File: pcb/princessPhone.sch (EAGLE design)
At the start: 75 parts, among them IC1 OPA2134UA, P2 TC2030-MCP-NL, Q1 2N7002K, SW3 LL1105BF250Q, SW4 LL1105BF250Q, SW5 LL1105BF250Q, SW6 LL1105BF250Q, U1 AG1170-S3-VERTICAL, U2 PI32MX170D-PT, U3 BLUETOOTH-RN-52, U4 V_REG_LD1085D2, X1 22-23-2041, X2 XRJK-S-01-6-4-0-9M2, X3 USB_MICRO_B

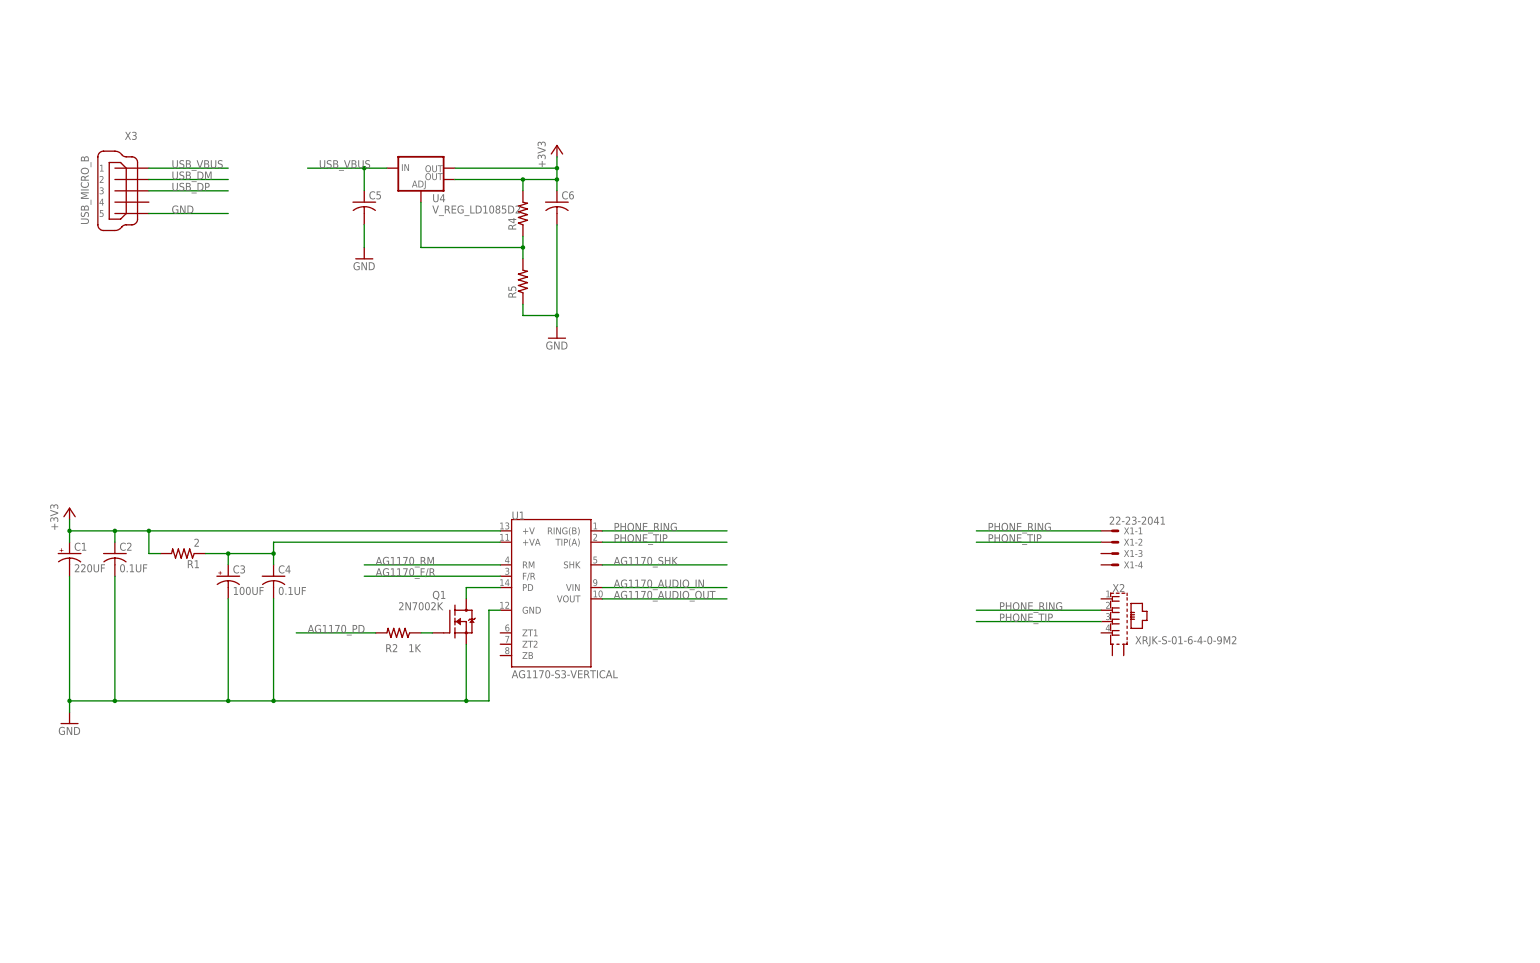
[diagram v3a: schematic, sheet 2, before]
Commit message: Replaced leo with switcher, finished first-pass layout, added LEDs.
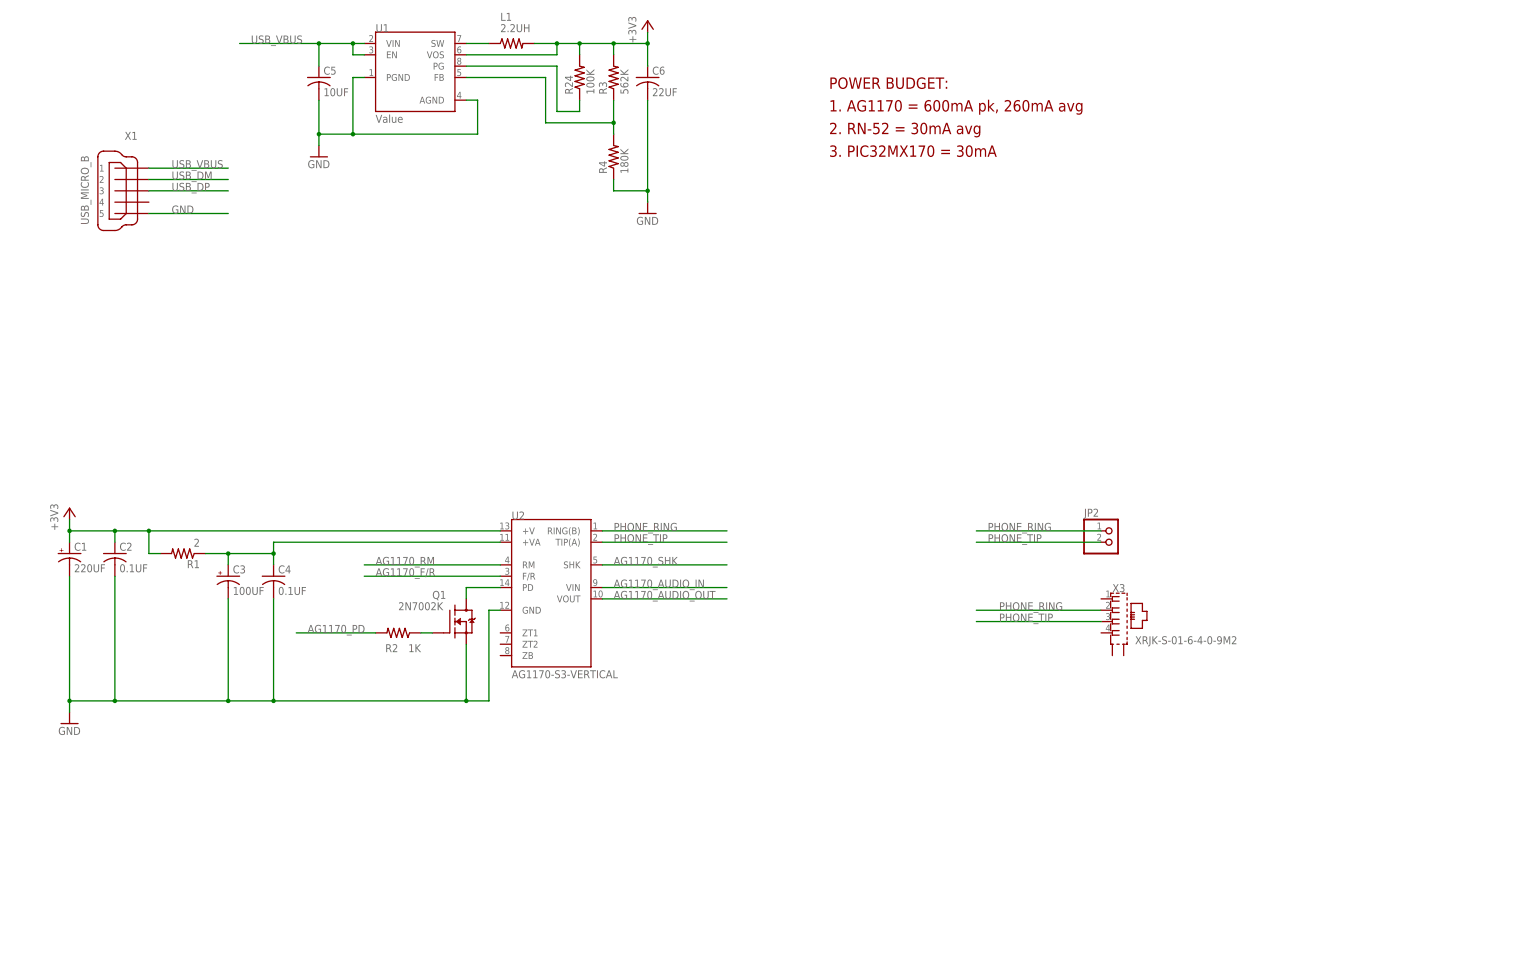
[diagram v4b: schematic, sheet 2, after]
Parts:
- removed C28: 0.1UF, rcl:C-USC0402
- removed IC1: OPA2134UA, linear:OPA2134UA
- removed R27, R28, R29: 10K, rcl:R-US_R0603
- removed SW5, SW6: LL1105BF250Q, raveGearControl:LL1105BF250Q
- removed TP3: PTR1B1,27, testpad:PTR1B1,27
- removed X2: XRJK-S-01-6-4-0-9M2, con-xmultiple:XRJK-S-01-6-4-0-9M2
- added C8: 0.1UF, rcl:C-USC0402
- added JP2: (no value), pinhead:PINHD-1X2
- added L1: 2.2UH, rcl:R-US_R0805
- added LED3: BLUE, led:LEDCHIPLED_0603
- added LED4: RED, led:LEDCHIPLED_0603
- added SW1, SW2: LL1105BF250Q, raveGearControl:LL1105BF250Q
- C2, C4: device rcl:C-USC0805 -> rcl:C-USC0603
- C5: value (none) -> 10UF; device rcl:C-USC0603 -> rcl:C-USC0805
- C6: value (none) -> 22UF; device rcl:C-USC0603 -> rcl:C-USC1206
- R10: value NP -> 10K
- R11: value 47K -> 10K
- R13: value NP -> 47K
- R14, R20, R21: value NP -> 0
- R15, R16, R17: value 47 -> 0
- R19: value NP -> 470
- R24: value 0 -> 100K
- R25: value 0 -> 47
- R26: value 10K -> 470
- R3: value 10K -> 562K; device rcl:R-US_R0402 -> rcl:R-US_R0603
- R4: value (none) -> 180K
- R5: value (none) -> 10K; device rcl:R-US_R0603 -> rcl:R-US_R0402
- R7: value 47 -> 10K; device rcl:R-US_R0603 -> rcl:R-US_R0402
- R8: device rcl:R-US_R0402 -> rcl:R-US_R0603
- R9: value 470 -> 10K
- U1: value AG1170-S3-VERTICAL -> Value; device princessPhone:AG1170-S3-VERTICAL -> princessPhone:TPS62160DGKR
- U2: value PI32MX170D-PT -> AG1170-S3-VERTICAL; device raveGear5:PI32MX170D-PT -> princessPhone:AG1170-S3-VERTICAL
- U3: value BLUETOOTH-RN-52 -> PI32MX170D-PT; device SparkFun-RF:BLUETOOTH-RN-52 -> raveGear5:PI32MX170D-PT
- U4: value V_REG_LD1085D2 -> BLUETOOTH-RN-52; device SparkFun-PowerIC:V_REG_LD1085D2 -> SparkFun-RF:BLUETOOTH-RN-52
- X1: value 22-23-2041 -> USB_MICRO_B; device con-molex:22-23-2041 -> FosBattery1:USB_MICRO_B
- X3: value USB_MICRO_B -> XRJK-S-01-6-4-0-9M2; device FosBattery1:USB_MICRO_B -> con-xmultiple:XRJK-S-01-6-4-0-9M2
- renumbered C26 to C7, C27 to C9, P2 to P1
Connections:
- removed net PIC32_RSVD_10: TP3.TP, U2PORTB.RPB9/SDA1/CTED4/PMD3/RB9
- removed net RN52_SPKR_SUM: IC1A.+IN, R13.2, R14.2, R15.1
- new net N$5: L1.1, U1.SW
- new net N$6: R24.1, U1.PG
- new net N$7: LED3.C, R25.2
- net +3V3: now also C8.1, L1.2, LED3.A, LED4.A, R10.1, R11.1, R24.2, R5.2, R7.2, R8.1, R9.1, U1.VOS, U2.+V, U3PWR.AVDD, U3PWR.VDD@1, U3PWR.VDD@2, U4.VDD; no longer C28.1, IC1A.V+, R26.1, R27.1, R28.1, R29.1, R4.2, R8.2, U1.+V, U2PWR.AVDD, U2PWR.VDD@1, U2PWR.VDD@2, U3.VDD, U4.OUT, U4.OUT@1
- net AG1170_AUDIO_IN: now also U2.VIN; no longer IC1A.OUT, R15.2, U1.VIN
- net AG1170_AUDIO_OUT: now also R20.2, R21.2, U2.VOUT; no longer IC1B.+IN, R18.2, R24.2, R25.2, U1.VOUT
- net AG1170_F/R: now also U2.F/R, U3PORTC.RPC4/PMA4/RC4; no longer U1.F/R, U2PORTC.RPC4/PMA4/RC4
- net AG1170_PD: now also U3PORTC.RPC6/PMA1/RC6; no longer U2PORTC.RPC6/PMA1/RC6
- net AG1170_RM: now also U2.RM, U3PORTC.RPC3/RC3; no longer U1.RM, U2PORTC.RPC3/RC3
- net AG1170_SHK: now also U2.SHK, U3PORTC.RPC5/PMA3/RC5; no longer U1.SHK, U2PORTC.RPC5/PMA3/RC5
- net GND: now also C8.2, R13.1, R14.2, R15.2, R16.2, R17.2, R4.1, SW1.P, SW2.P, U1.AGND, U1.PGND, U2.GND, U3PWR.AVSS, U3PWR.VSS@1, U3PWR.VSS@2, U3PWR.VSS@3, U4.AGND, U4.GND, U4.GND1, U4.GND2, U4.GND3, U4.GND4, U4.GND5, U4.GND6, U4.GND7, U4.GND8, U4.GND9, X1.5; no longer C28.2, IC1A.-IN, IC1A.V-, IC1B.-IN, R10.2, R11.1, R19.2, R20.2, R21.2, R5.1, SW5.P, SW6.P, U1.GND, U2PWR.AVSS, U2PWR.VSS@1, U2PWR.VSS@2, U2PWR.VSS@3, U3.AGND, U3.GND, U3.GND1, U3.GND2, U3.GND3, U3.GND4, U3.GND5, U3.GND6, U3.GND7, U3.GND8, U3.GND9, X3.5
- net LED0: now also R18.1, U4.LED0; no longer R7.1, U3.LED0
- net LED1: now also R19.1, U4.LED1; no longer R9.1, U3.LED1
- net MCLR#: now also R5.1, U3PWR.#MCLR; no longer R3.1, U2PWR.#MCLR
- net N$1: now also U2.+VA; no longer U1.+VA
- net N$10: now also R19.2; no longer R9.2
- net N$11: now also U4.MIC_BIAS; no longer U3.MIC_BIAS
- net N$12: now also LED4.C, R26.2; no longer IC1B.OUT, R16.2, R17.2, R18.1
- net N$3: now also U2.PD; no longer U1.PD
- net N$4: now also U3PWR.VCAP; no longer U2PWR.VCAP
- net N$8: now also R3.1, R4.2, U1.FB; no longer R4.1, R5.2, U4.ADJ
- net N$9: now also R18.2; no longer R7.2
- net PHONE_RING: now also JP2.1, U2.RING(B), X3.2; no longer U1.RING(B), X1-1.S, X2.2
- net PHONE_TIP: now also JP2.2, U2.TIP(A), X3.3; no longer U1.TIP(A), X1-2.S, X2.3
- net PIC32_PGEC1: now also U3PORTB.PGEC1/AN3/C1INC/C2INA/RPB1/CTED12/RB1; no longer U2PORTB.PGEC1/AN3/C1INC/C2INA/RPB1/CTED12/RB1
- net PIC32_PGED1: now also U3PORTB.PGED1/AN2/C1IND/C2INB/C3IND/RPB0/RB0; no longer U2PORTB.PGED1/AN2/C1IND/C2INB/C3IND/RPB0/RB0
- net PIC32_RSVD_1: now also U3PORTA.VREF+/CVREF+/AN0/C3INC/RPA0/CTED1/RA0; no longer U2PORTA.VREF+/CVREF+/AN0/C3INC/RPA0/CTED1/RA0
- net PIC32_RSVD_11: now also U3PORTB.PGEC2/RPB11/PMD1/RB11; no longer U2PORTB.PGEC2/RPB11/PMD1/RB11
- net PIC32_RSVD_12: now also U3PORTB.CVREFOUT/AN10/C3INB/RPB14/SCK1/CTED5/PMWR/RB14; no longer U2PORTB.CVREFOUT/AN10/C3INB/RPB14/SCK1/CTED5/PMWR/RB14
- net PIC32_RSVD_2: now also U3PORTA.OSC1/CLKI/RPA2/RA2; no longer U2PORTA.OSC1/CLKI/RPA2/RA2
- net PIC32_RSVD_3: now also U3PORTA.OSC2/CLKO/RPA3/RA3; no longer U2PORTA.OSC2/CLKO/RPA3/RA3
- net PIC32_RSVD_4: now also U3PORTA.SOSCO/RPA4/T1CK/CTED9/RA4; no longer U2PORTA.SOSCO/RPA4/T1CK/CTED9/RA4
- net PIC32_RSVD_5: now also R26.1, U3PORTA.PGEC/TCK/CTED8/PMA7/RA7; no longer U2PORTA.PGEC/TCK/CTED8/PMA7/RA7
- net PIC32_RSVD_6: now also U3PORTA.TDO/RPA8/PMA8/RA8; no longer U2PORTA.TDO/RPA8/PMA8/RA8
- net PIC32_RSVD_7: now also U3PORTA.TDI/RPA9/PMA9/RA9; no longer U2PORTA.TDI/RPA9/PMA9/RA9
- net PIC32_RSVD_8: now also R25.1, U3PORTA.PGED/TMS/PMA10/RA10; no longer U2PORTA.PGED/TMS/PMA10/RA10
- net PIC32_RSVD_9: now also U3PORTB.SOSCI/RPB4/RB4; no longer U2PORTB.SOSCI/RPB4/RB4
- net PIC32_SCL2: now also R7.1, U3PORTB.AN5/C1INA/C2INC/RTCC/RPB3/SCL2/RB3; no longer R8.1, U2PORTB.AN5/C1INA/C2INC/RTCC/RPB3/SCL2/RB3
- net PIC32_SDA2: now also U3PORTB.AN4/C1INB/C2IND/RPB2/SDA2/CTED13/RB2; no longer U2PORTB.AN4/C1INB/C2IND/RPB2/SDA2/CTED13/RB2
- net PIC32_U1CTS#_3V3: now also U3PORTA.VREF-/CVREF-/AN1/RPA1/CTED2/RA1, U4.UART_RTS; no longer U2PORTA.VREF-/CVREF-/AN1/RPA1/CTED2/RA1, U3.UART_RTS
- net PIC32_U1RTS#_3V3: now also U3PORTB.PGED2/RPB10/CTED11/PMD2/RB10, U4.UART_CTS; no longer U2PORTB.PGED2/RPB10/CTED11/PMD2/RB10, U3.UART_CTS
- net PIC32_U1RX_3V3: now also U3PORTC.AN7/RPC1/RC1, U4.UART_TX; no longer U2PORTC.AN7/RPC1/RC1, U3.UART_TX
- net PIC32_U1TX_3V3: now also U3PORTC.AN6/RPC0/RC0, U4.UART_RX; no longer U2PORTC.AN6/RPC0/RC0, U3.UART_RX
- net RN52_CMD_MODE#: now also U3PORTC.RPC9/CTED7/PMA6/RC9, U4.GPIO9; no longer U2PORTC.RPC9/CTED7/PMA6/RC9, U3.GPIO9
- net RN52_DFU_MODE: now also R13.2, U3PORTB.RPB9/SDA1/CTED4/PMD3/RB9, U4.GPIO3; no longer R11.2, U3.GPIO3
- net RN52_EVENT#: now also U3PORTC.RPC8/PMA5/RC8, U4.GPIO2; no longer U2PORTC.RPC8/PMA5/RC8, U3.GPIO2
- net RN52_FACTORY_RST: now also U4.GPIO4; no longer U3.GPIO4
- net RN52_MIC_L+: now also R20.1, U4.MIC_L+; no longer R16.1, R24.1, R25.1, U3.MIC_L+
- net RN52_MIC_L-: now also R17.1, U4.MIC_L-; no longer R21.1, U3.MIC_L-
- net RN52_MIC_R+: now also R21.1, U4.MIC_R+; no longer R17.1, U3.MIC_R+
- net RN52_MIC_R-: now also R16.1, U4.MIC_R-; no longer R20.1, U3.MIC_R-
- net RN52_PWREN: now also U3PORTC.RPC7/PMA0/RC7, U4.PWREN; no longer U2PORTC.RPC7/PMA0/RC7, U3.PWREN
- net RN52_SPKR_L+: now also U4.SPKR_L+; no longer R13.1, U3.SPKR_L+
- net RN52_SPKR_L-: now also R14.1, U4.SPKR_L-; no longer R10.1, U3.SPKR_L-
- net RN52_SPKR_R+: now also U4.SPKR_R+; no longer R14.1, U3.SPKR_R+
- net RN52_SPKR_R-: now also R15.1, U4.SPKR_R-; no longer R19.1, U3.SPKR_R-
- net SST25_CE#: now also U3PORTB.AN12/PMD0/RB12; no longer U2PORTB.AN12/PMD0/RB12
- net SST25_MISO: now also U3PORTC.AN8/RPC2/PMA2/RC2; no longer U2PORTC.AN8/RPC2/PMA2/RC2
- net SST25_MOSI: now also U3PORTB.AN11/RPB13/CTPLS/PMRD/RB13; no longer U2PORTB.AN11/RPB13/CTPLS/PMRD/RB13
- net SST25_SCK: now also U3PORTB.AN9/C3INA/RPB15/SCK2/CTED6/PMCS1/RB15; no longer U2PORTB.AN9/C3INA/RPB15/SCK2/CTED6/PMCS1/RB15
- net SW0: now also R8.2, SW1.S, U3PORTB.PGED3/RPB5/PMD7/RB5; no longer R26.2, SW3.S, U2PORTB.PGED3/RPB5/PMD7/RB5
- net SW1: now also R9.2, SW2.S, U3PORTB.PGEC3/RPB6/PMD6/RB6; no longer R27.2, SW4.S, U2PORTB.PGEC3/RPB6/PMD6/RB6
- net SW2: now also R10.2, SW3.S, U3PORTB.RPB7/CTED3/PMD5/INT0/RB7; no longer R28.2, SW5.S, U2PORTB.RPB7/CTED3/PMD5/INT0/RB7
- net SW3: now also R11.2, SW4.S, U3PORTB.RPB8/SCL1/CTED10/PMD4/RB8; no longer R29.2, SW6.S, U2PORTB.RPB8/SCL1/CTED10/PMD4/RB8
- net USB_DM: now also U4.USBD-, X1.2; no longer U3.USBD-, X3.2
- net USB_DP: now also U4.USBD+, X1.3; no longer U3.USBD+, X3.3
- net USB_VBUS: now also U1.EN, X1.1; no longer U4.IN, X3.1
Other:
- note added: "1. AG1170 = 600mA pk, 260mA avg"
- note added: "2. RN-52 = 30mA avg"
- note added: "2015.08.06"
- note added: "3. PIC32MX170 = 30mA"
- note added: "FIRST-PASS AT LAYOUT, REMOVED "NP" COMPONENTS, REPLACED LDO WITH SWITCHER, ADDED LEDS"
- note added: "POWER BUDGET:"
- note removed: "STUFF OPTION 2"
- moved on the sheet: C10, C5, C6, R13, R14, R15, R16, R17, R18, R19, R20, R21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

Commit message: FIRST PASS AT LAYOUT
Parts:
- removed TP4: PTR1B1,27, testpad:PTR1B1,27
- added TP3: PTR1B1,27, testpad:PTR1B1,27
- JP1: device pinhead:PINHD-1X3 -> pinhead:PINHD-1X4
- LED3: value BLUE -> GREEN
- LED4: value RED -> YELLOW
- R25: value 47 -> 150
- R26: value 470 -> 150
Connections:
- removed net AG1170_AUDIO_IN_AGG: R22.1, R23.2
- removed net PIC32_RSVD_11: TP4.TP, U3PORTB.PGEC2/RPB11/PMD1/RB11
- net +3V3: now also JP1.1
- net AG1170_AUDIO_IN: now also R22.1, R23.2
- net GND: now also JP1.4; no longer JP1.1
- net PHONE_RING: now also X3.3; no longer X3.2
- net PHONE_TIP: now also X3.2; no longer X3.3
- net PIC32_U1RX_3V3: now also JP1.3; no longer JP1.2
- net PIC32_U1TX_3V3: now also JP1.2; no longer JP1.3
- net RN52_FACTORY_RST: now also U3PORTB.PGEC2/RPB11/PMD1/RB11
- net RN52_SPKR_R+: now also TP3.TP
- net USB_VBUS: now also U1.VIN
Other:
- note added: "4. LEDS = 10mA * 4 = 40mA"
- note added: "CONNECTED RN52 FACTORY RST LINE, CORRECTED RJ-11 PINOUT"
- note added: "FIRST-PASS AT LAYOUT"
- note added: "FIRST-PASS AT PLACEMENT, REMOVED "NP" COMPONENTS, REPLACED LDO WITH SWITCHER, ADDED LEDS"
- note removed: "FIRST-PASS AT LAYOUT, REMOVED "NP" COMPONENTS, REPLACED LDO WITH SWITCHER, ADDED LEDS"
- moved on the sheet: LED3, LED4, R25, R26

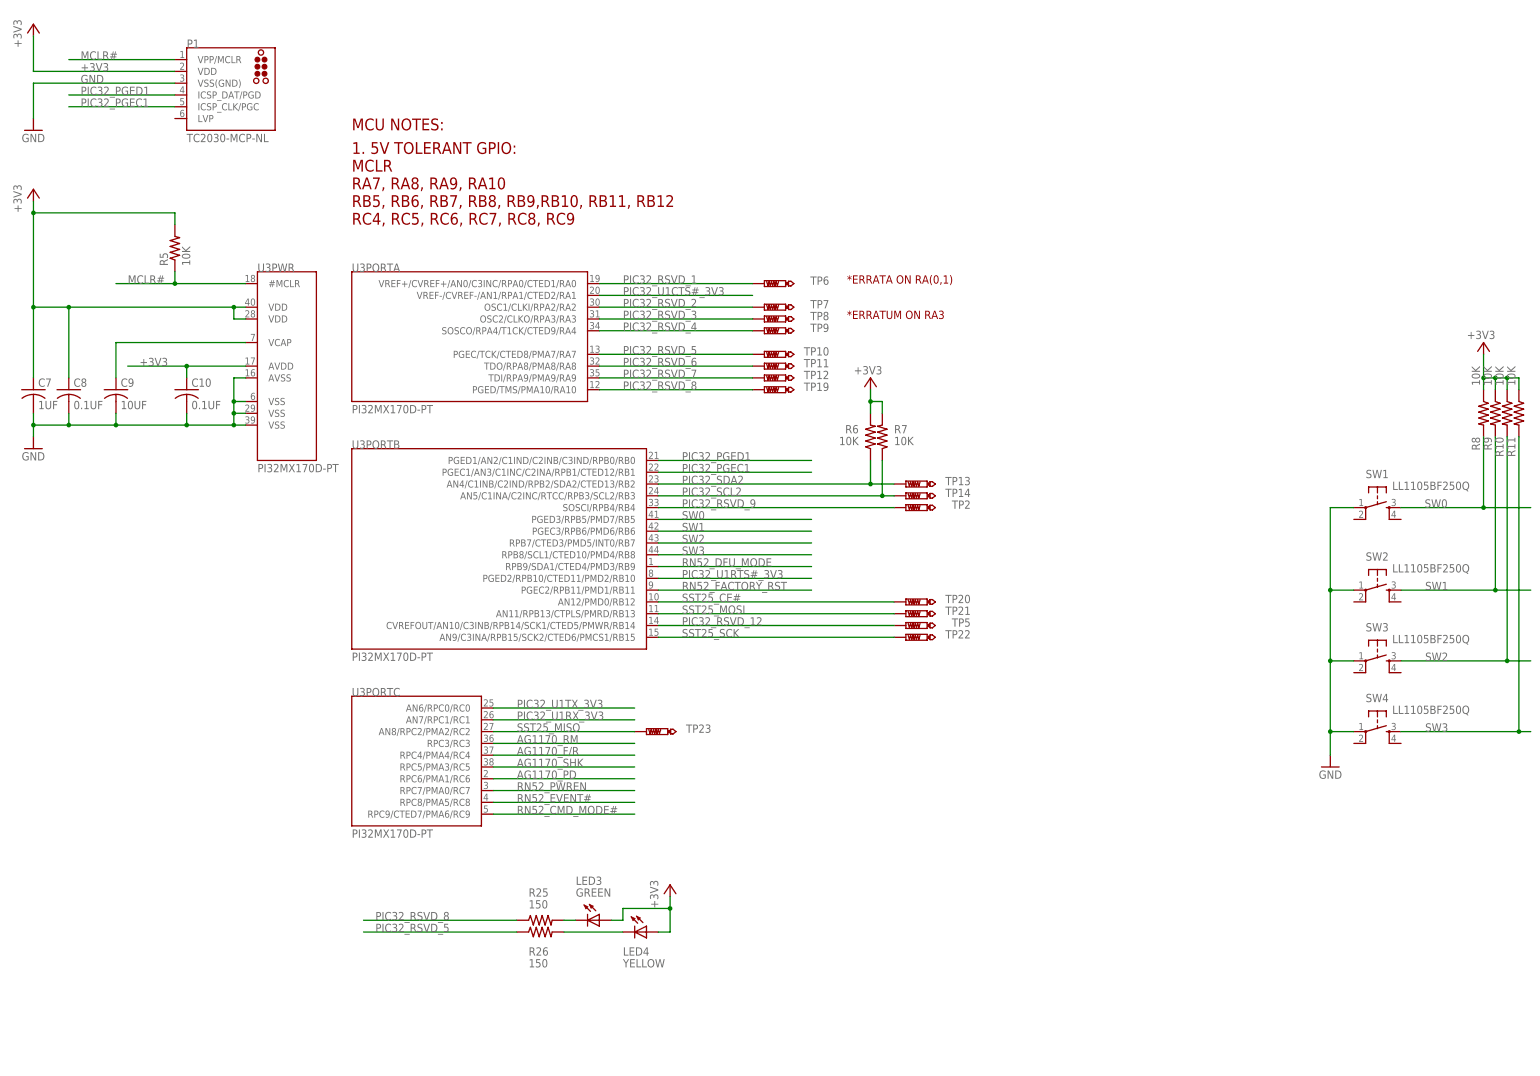
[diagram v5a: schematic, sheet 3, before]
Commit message: REMOVED BTN, ADDING LEDS, ADDED OUTLINE
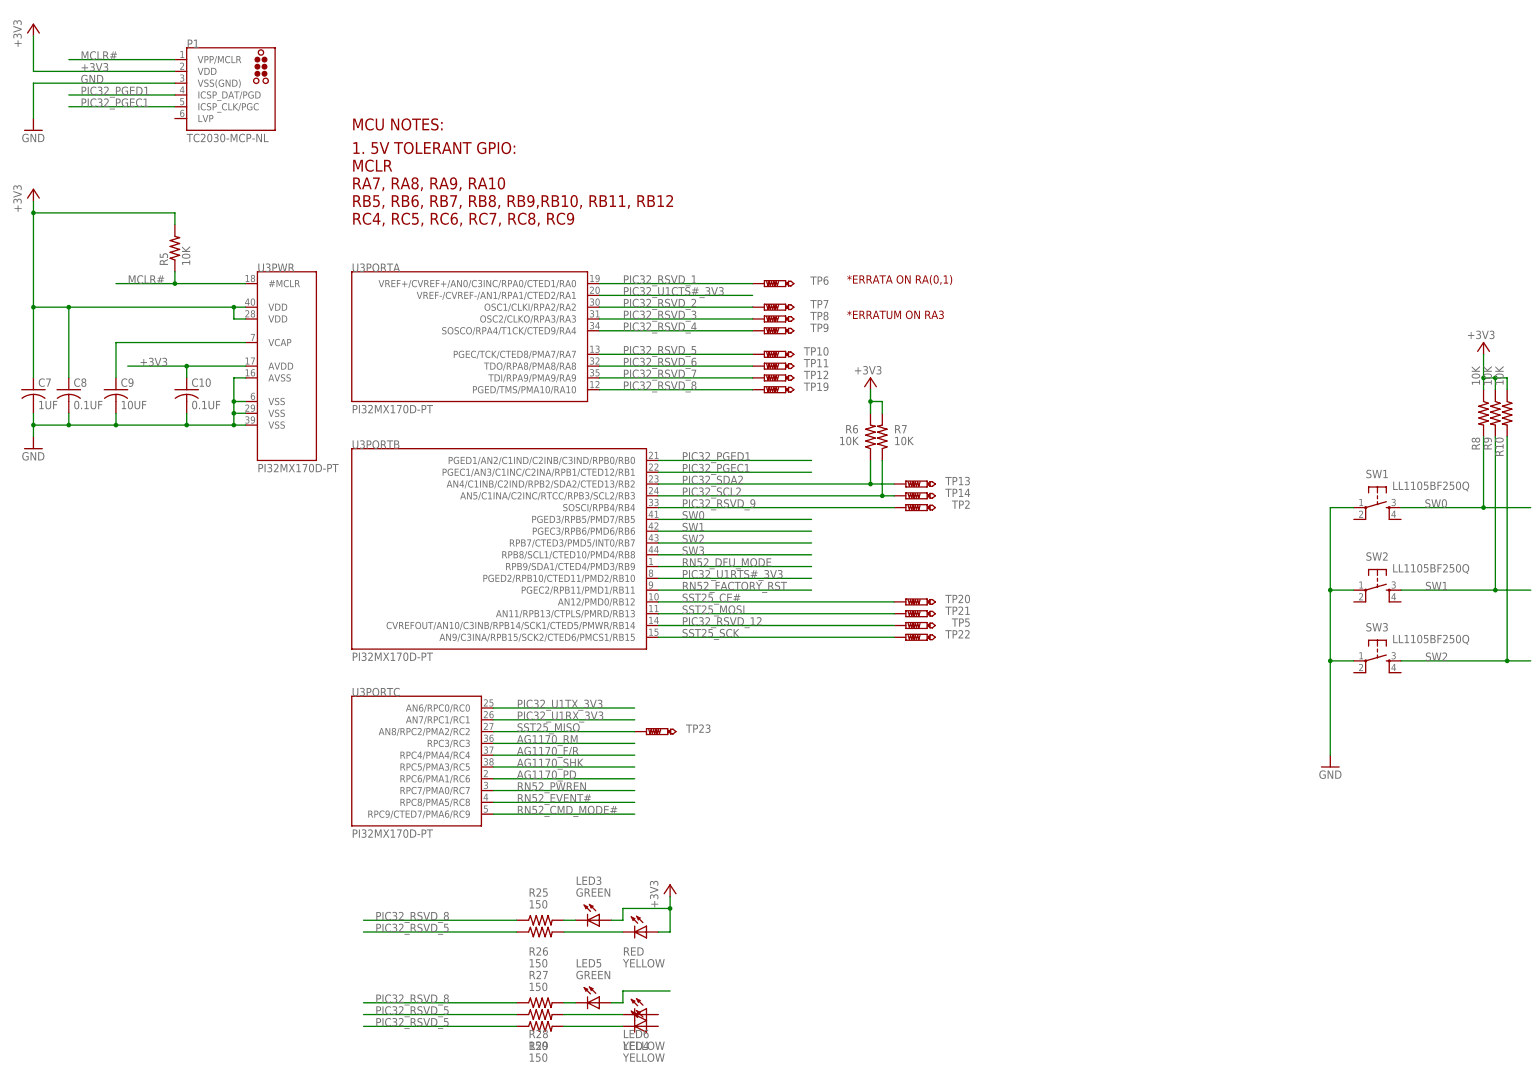
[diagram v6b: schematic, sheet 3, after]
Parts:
- removed R11: 10K, rcl:R-US_R0603
- removed SW4: LL1105BF250Q, raveGearControl:LL1105BF250Q
- added E1: 1591XXMS, princessPhone:1591XXMS
- added LED5: GREEN, led:LEDCHIPLED_0603
- added LED6, RED: YELLOW, led:LEDCHIPLED_0603
- added R27, R28, R29: 150, rcl:R-US_R0603
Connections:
- net N$1 renamed +VA
- new net +3V1: LED5.A
- new net N$1: LED5.C, R27.2
- new net N$13: LED6.C, R28.2
- new net N$14: LED4.C, R29.2
- net +3V3: now also RED.A; no longer LED4.A, R11.1
- net GND: no longer SW4.P
- net N$12: now also RED.C; no longer LED4.C
- net PIC32_RSVD_5: now also R28.1, R29.1
- net PIC32_RSVD_8: now also R27.1
- net SW3: no longer R11.2, SW4.S
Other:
- note added: "2015.08.07"
- note added: "2015.08.08"
- note added: "REMOVED A BUTTON, ADDING RGB LED FOR FUNCTION AND RED/GREEN FOR STATUS, ADDED ENCLOSURE PCB OUTLINE"
- moved on the sheet: LED4

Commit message: FINISHED ROUTING
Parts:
- removed RED: YELLOW, led:LEDCHIPLED_0603
- added LED7: GREEN, led:LEDCHIPLED_0603
- LED3, LED5: value GREEN -> RED
- LED4: value YELLOW -> BLUE
- LED6: value YELLOW -> GREEN
- SW1, SW2, SW3: value LL1105BF250Q -> (none); device raveGearControl:LL1105BF250Q -> switch-omron:31-XX
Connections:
- removed net +3V1: LED5.A
- net +3V3: now also LED4.A, LED5.A, LED6.A, LED7.A; no longer RED.A
- net N$12: now also LED7.C; no longer RED.C
- net PIC32_RSVD_1: now also R28.1
- net PIC32_RSVD_12: now also R27.1
- net PIC32_RSVD_2: now also R29.1
- net PIC32_RSVD_5: no longer R28.1, R29.1
- net PIC32_RSVD_8: no longer R27.1
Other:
- note added: "2015.08.09"
- note added: "FINISHED ROUTING"
- moved on the sheet: LED3, LED4, LED5, LED6, R26, R28, R29
